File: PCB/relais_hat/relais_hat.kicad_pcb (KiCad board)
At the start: 4 copper layers, 85 x 56 mm, 61 parts, among them J1 Conn_01x03, J10 Conn_01x02, J11 Conn_01x02, J12 Conn_01x03, J13 DB9_Female, J14 Conn_01x02, J15 Conn_01x02, J16 Conn_01x02, J17 Conn_01x02, J18 Conn_01x02, J2 Conn_01x03, J3 Conn_02x04_Odd_Even, J4 Screw_Terminal_01x02, J5 Screw_Terminal_01x02, J6 Screw_Terminal_01x02, J7 Screw_Terminal_01x02, J8 Conn_01x02, J9 Conn_01x02, K1 RELAY-HLS8L-DC3V-S-C(5P-19X15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, K2 RELAY-HLS8L-DC3V-S-C(5P-19X15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, K3 RELAY-HLS8L-DC3V-S-C(5P-19X15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, K4 RELAY-HLS8L-DC3V-S-C(5P-19X15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, P1 Conn_02x20_Odd_Even, Q1 S8050, Q2 S8050, Q3 S8050, Q4 S8050, U1 XC6206P302MR-G, U2 XC6206P302MR-G, U3 XC6206P302MR-G, U4 XC6206P302MR-G

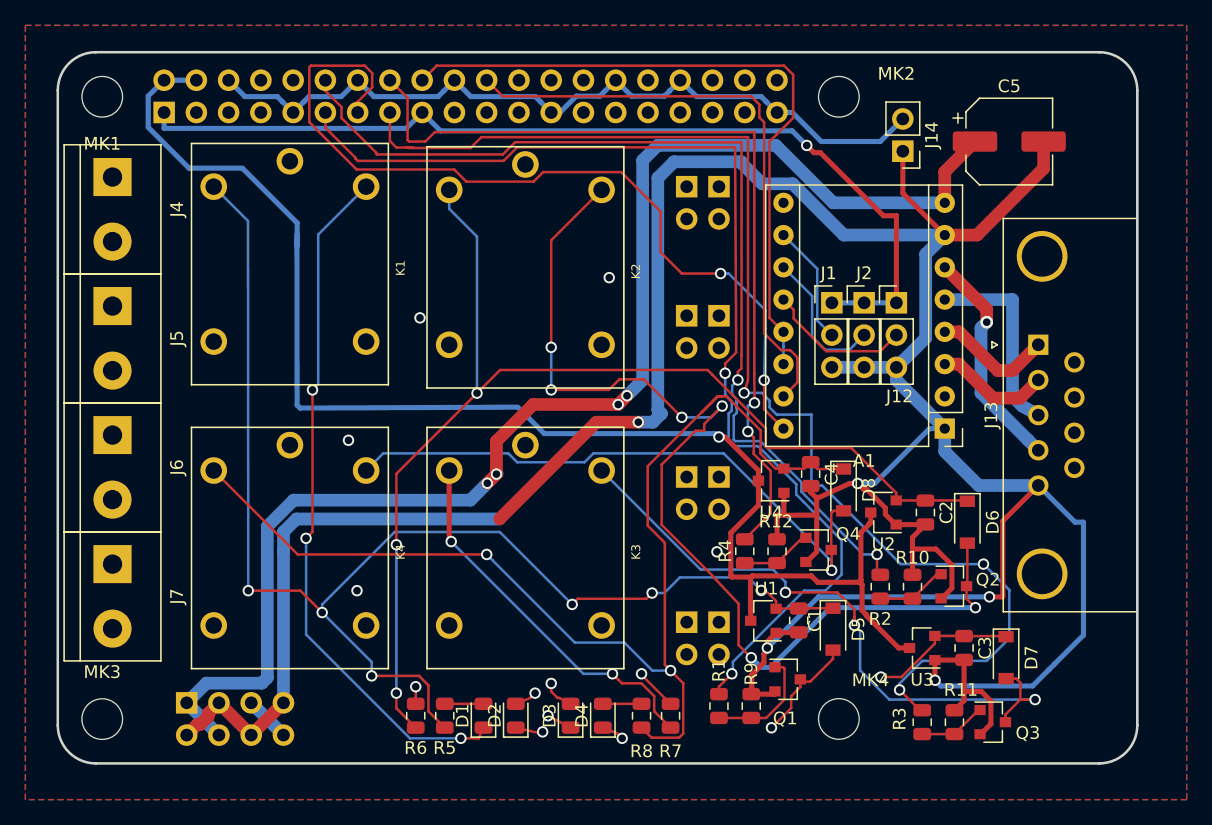
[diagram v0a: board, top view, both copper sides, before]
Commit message: add 3D xt30 model
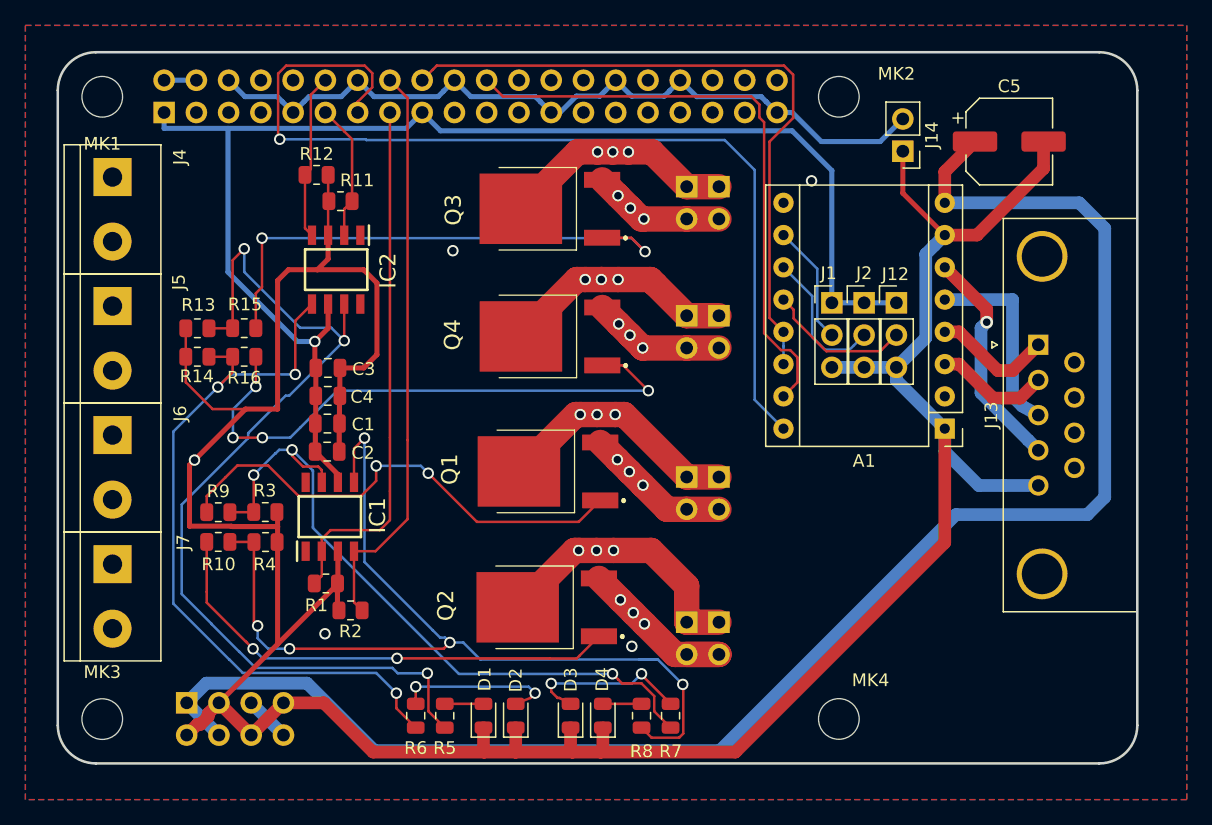
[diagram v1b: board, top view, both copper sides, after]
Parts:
- removed D5, D6, D7, D8: 1N4148W-7-F, Diode_SMD:D_SOD-123
- removed K1, K2, K3, K4: RELAY-HLS8L-DC3V-S-C(5P-19X15MM), relais:REY5-19.0X15.0X15.0MM
- removed U1, U2, U3, U4: XC6206P302MR-G, Package_TO_SOT_SMD:SOT-23
- added IC1: UCC27324D, UCC27324D:SOIC127P600X175-8N, F.Cu at (221.4, 130.3)
- added IC2: UCC27324D, UCC27324D:SOIC127P600X175-8N, F.Cu at (221.9, 110.8)
- added R13: 10k, Resistor_SMD:R_0805_2012Metric, F.Cu at (211.0, 115.4)
- added R14: 10k, Resistor_SMD:R_0805_2012Metric, F.Cu at (211.0, 117.7)
- added R15: 100, Resistor_SMD:R_0805_2012Metric, F.Cu at (214.7, 115.4)
- added R16: 100, Resistor_SMD:R_0805_2012Metric, F.Cu at (214.7, 117.7)
- C1, C3: value 1uF -> 0.1uF
- Q1, Q2, Q3, Q4: value S8050 -> FDD8447L-F085; footprint Package_TO_SOT_SMD:SOT-23 -> FDD8447L:FDD8447LF085
- R1, R2, R3, R4: value 4.7k -> 10k
- R10, R9: value 47k -> 100
- R11, R12: value 47k -> 10k
- moved R11 63.4 mm to (222.3, 105.4), turned to 0 degrees
- moved R10 54.8 mm to (212.7, 132.2), turned to 0 degrees
- moved C3 54.7 mm to (221.3, 118.5), turned to 0 degrees
- moved R3 54.3 mm to (216.3, 129.9), turned to 180 degrees
- moved Q3 53.4 mm to (238.8, 106.0), turned to 90 degrees
- moved C2 47.3 mm to (221.2, 125.1), turned to 0 degrees
- moved R12 46.8 mm to (220.4, 103.3), turned to 0 degrees
- moved R9 44.7 mm to (212.7, 129.9), turned to 0 degrees
- moved R2 41.8 mm to (223.1, 137.6), turned to 180 degrees
- moved C1 40.2 mm to (221.2, 122.9), turned to 0 degrees
- moved C4 38.5 mm to (221.3, 120.8), turned to 0 degrees
- moved R4 37.7 mm to (216.4, 132.3), turned to 0 degrees
- moved R1 32.4 mm to (221.1, 135.5), turned to 180 degrees
- moved Q2 32.0 mm to (238.6, 137.4), turned to 90 degrees
- moved Q4 27.0 mm to (238.8, 116.1), turned to 90 degrees
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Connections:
- A1 pad 2: (no net) -> Net-(A1-Pad2)
- A1 pad 9: (no net) -> Net-(A1-Pad9)
- C1 pad 1: Net-(C1-Pad1) -> +3V3
- C2 pad 1: Net-(C2-Pad1) -> +3V3
- C3 pad 1: Net-(C3-Pad1) -> +3V3
- C4 pad 1: Net-(C4-Pad1) -> +3V3
- D1 pad 1: Net-(D1-Pad1) -> GND
- D2 pad 1: Net-(D2-Pad1) -> GND
- D3 pad 1: Net-(D3-Pad1) -> GND
- D4 pad 1: Net-(D4-Pad1) -> GND
- J13 pad 6: (no net) -> Net-(J13-Pad6)
- J13 pad 7: (no net) -> Net-(J13-Pad7)
- J13 pad 8: (no net) -> Net-(J13-Pad8)
- J13 pad 9: (no net) -> Net-(J13-Pad9)
- P1 pad 10: (no net) -> /UART_RX
- P1 pad 19: (no net) -> /UART_TX_NanopiM4
- P1 pad 21: (no net) -> /UART_RX_NanopiM4
- P1 pad 23: (no net) -> Net-(P1-Pad23)
- P1 pad 24: (no net) -> Net-(P1-Pad24)
- P1 pad 26: (no net) -> Net-(P1-Pad26)
- P1 pad 27: (no net) -> Net-(P1-Pad27)
- P1 pad 28: (no net) -> Net-(P1-Pad28)
- P1 pad 29: (no net) -> Net-(P1-Pad29)
- P1 pad 3: (no net) -> /SDA
- P1 pad 31: (no net) -> Net-(P1-Pad31)
- P1 pad 32: (no net) -> Net-(P1-Pad32)
- P1 pad 33: (no net) -> Net-(P1-Pad33)
- P1 pad 35: (no net) -> Net-(P1-Pad35)
- P1 pad 36: (no net) -> Net-(P1-Pad36)
- P1 pad 37: (no net) -> Net-(P1-Pad37)
- P1 pad 38: (no net) -> Net-(P1-Pad38)
- P1 pad 40: (no net) -> Net-(P1-Pad40)
- P1 pad 5: (no net) -> /SCL
- P1 pad 7: (no net) -> /1-wire
- P1 pad 8: (no net) -> /UART_TX
- Q1 pad 2: GND -> Net-(J16-Pad1)
- Q1 pad 3: Net-(D1-Pad1) -> Net-(J16-Pad2)
- Q2 pad 2: GND -> Net-(J10-Pad1)
- Q2 pad 3: Net-(D2-Pad1) -> Net-(J10-Pad2)
- Q3 pad 2: GND -> Net-(J15-Pad1)
- Q3 pad 3: Net-(D3-Pad1) -> Net-(J15-Pad2)
- Q4 pad 2: GND -> Net-(J11-Pad1)
- Q4 pad 3: Net-(D4-Pad1) -> Net-(J11-Pad2)
- R1 pad 1: /GPIO17 -> GND
- R1 pad 2: Net-(Q1-Pad1) -> /GPIO22
- R10 pad 2: GND -> Net-(IC1-Pad5)
- R11 pad 1: Net-(Q3-Pad1) -> GND
- R11 pad 2: GND -> /GPIO17
- R12 pad 1: Net-(Q4-Pad1) -> /GPIO18
- R2 pad 1: /GPIO18 -> /GPIO23
- R2 pad 2: Net-(Q2-Pad1) -> GND
- R3 pad 1: /GPIO22 -> GND
- R3 pad 2: Net-(Q3-Pad1) -> Net-(IC1-Pad7)
- R4 pad 1: /GPIO23 -> Net-(IC1-Pad5)
- R4 pad 2: Net-(Q4-Pad1) -> GND
- R5 pad 1: Net-(C1-Pad1) -> Net-(IC2-Pad7)
- R6 pad 1: Net-(C2-Pad1) -> Net-(IC2-Pad5)
- R7 pad 1: Net-(C3-Pad1) -> Net-(IC1-Pad7)
- R8 pad 1: Net-(C4-Pad1) -> Net-(IC1-Pad5)
- R9 pad 2: GND -> Net-(IC1-Pad7)
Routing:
- net +5V: track 114.6 -> 2.54 mm, vias 1 -> 0
- net Net-(D2-Pad1): track 106.5 -> 0.00 mm, vias 7 -> 0
- net Net-(C1-Pad1): track 102.7 -> 0.00 mm, vias 6 -> 0
- net Net-(C4-Pad1): track 93.1 -> 0.00 mm, vias 2 -> 0
- net Net-(C2-Pad1): track 91.4 -> 0.00 mm, vias 3 -> 0
- net Net-(D1-Pad1): track 89.5 -> 0.00 mm, vias 4 -> 0
- net /GPIO17: track 88.7 -> 10.8 mm, vias 2 -> 0
- net Net-(D3-Pad1): track 77.3 -> 0.00 mm, vias 4 -> 0
- net Net-(IC1-Pad5): track 0.00 -> 77.0 mm, vias 0 -> 5
- net Net-(IC2-Pad7): track 0.00 -> 75.5 mm, vias 0 -> 3
- net Net-(D4-Pad1): track 74.9 -> 0.00 mm, vias 2 -> 0
- net /GPIO18: track 78.5 -> 13.5 mm, vias 2 -> 0
- net Net-(C3-Pad1): track 64.5 -> 0.00 mm, vias 3 -> 0
- net Net-(IC2-Pad5): track 0.00 -> 59.7 mm, vias 0 -> 3
- net /GPIO22: track 99.5 -> 41.8 mm, vias 3 -> 0
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
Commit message: add temp 1-wire in db9 connector
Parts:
- added R17: 4.7k, Resistor_SMD:R_0805_2012Metric, F.Cu at (266.2, 129.3)
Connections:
- J13 pad 7: Net-(J13-Pad7) -> +3V3
- J13 pad 8: Net-(J13-Pad8) -> /1-wire
- J13 pad 9: Net-(J13-Pad9) -> GND
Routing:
- net /1-wire: track 0.00 -> 127.3 mm, vias 0 -> 3
- net +3V3: track 107.4 -> 142.7 mm
- net GND: track 245.6 -> 249.0 mm
- net /GPIO24: track 54.0 -> 51.2 mm
- net /rpi_gnd: track 62.1 -> 63.9 mm
- net /GPIO25: track 47.4 -> 46.0 mm

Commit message: add R 10k on source/gate
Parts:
- added R18: 10k, Resistor_SMD:R_0805_2012Metric, F.Cu at (251.9, 144.4)
- added R19: 10k, Resistor_SMD:R_0805_2012Metric, F.Cu at (251.5, 133.7)
- added R20: 10k, Resistor_SMD:R_0805_2012Metric, F.Cu at (250.6, 121.3)
- added R21: 10k, Resistor_SMD:R_0805_2012Metric, F.Cu at (251.2, 110.9)
- renumbered Q3 to Q1, Q4 to Q2, Q1 to Q3, Q2 to Q4
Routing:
- net Net-(Q4-Pad1): track 38.2 -> 49.0 mm
- net Net-(Q3-Pad1): track 38.4 -> 48.3 mm
- net Net-(Q1-Pad1): track 41.7 -> 46.4 mm
- net Net-(J11-Pad2): track 54.9 -> 59.5 mm
- net Net-(J16-Pad2): track 56.6 -> 60.8 mm
- net Net-(J15-Pad2): track 54.6 -> 58.7 mm
- net Net-(J10-Pad2): track 58.1 -> 61.7 mm
- net Net-(Q2-Pad1): track 45.9 -> 49.4 mm

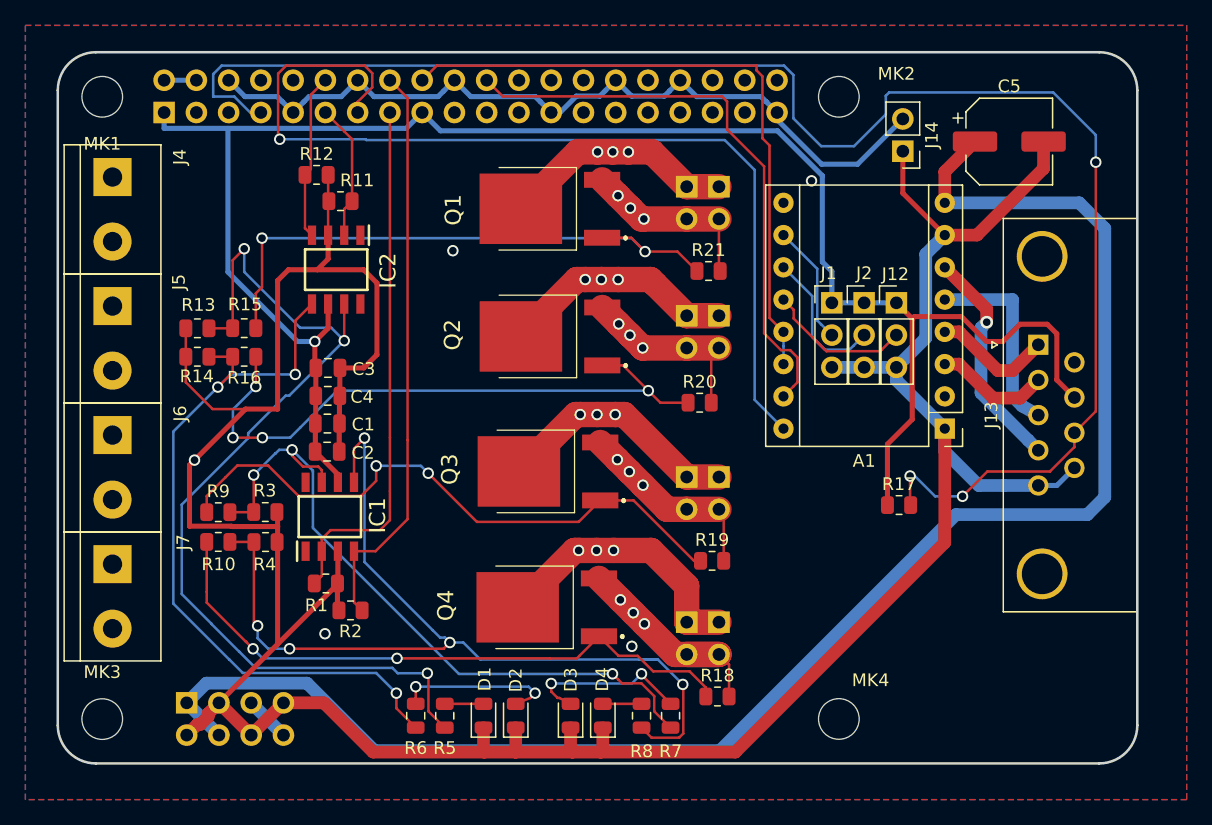
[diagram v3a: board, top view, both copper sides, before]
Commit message: upgrade relais hat and all hat to kicad 7.0
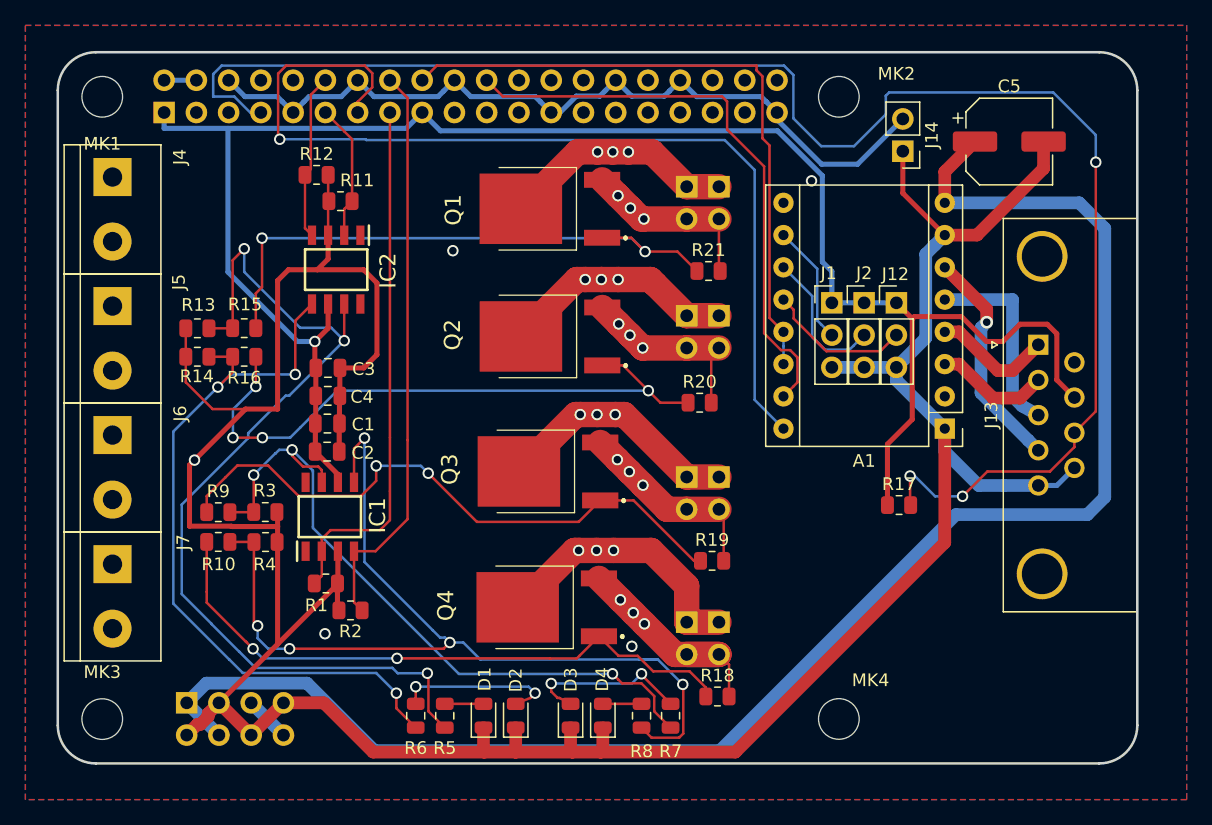
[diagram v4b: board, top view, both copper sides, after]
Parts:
- renumbered C5 to C
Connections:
- net +3V3 renamed +3.3V
- A1 pad 2: Net-(A1-Pad2) -> unconnected-(A1-~{FLT}-Pad2)
- A1 pad 9: Net-(A1-Pad9) -> unconnected-(A1-~{EN}-Pad9)
- IC1 pad 1: Net-(IC1-Pad1) -> unconnected-(IC1-N/A_1-Pad1)
- IC1 pad 8: Net-(IC1-Pad8) -> unconnected-(IC1-N/A_2-Pad8)
- IC2 pad 1: Net-(IC2-Pad1) -> unconnected-(IC2-N/A_1-Pad1)
- IC2 pad 8: Net-(IC2-Pad8) -> unconnected-(IC2-N/A_2-Pad8)
- J13 pad 0: (no net) -> GND
- J13 pad 6: Net-(J13-Pad6) -> unconnected-(J13-Pad6)
- P1 pad 23: Net-(P1-Pad23) -> unconnected-(P1-Pin_23-Pad23)
- P1 pad 24: Net-(P1-Pad24) -> unconnected-(P1-Pin_24-Pad24)
- P1 pad 26: Net-(P1-Pad26) -> unconnected-(P1-Pin_26-Pad26)
- P1 pad 27: Net-(P1-Pad27) -> unconnected-(P1-Pin_27-Pad27)
- P1 pad 28: Net-(P1-Pad28) -> unconnected-(P1-Pin_28-Pad28)
- P1 pad 29: Net-(P1-Pad29) -> unconnected-(P1-Pin_29-Pad29)
- P1 pad 31: Net-(P1-Pad31) -> unconnected-(P1-Pin_31-Pad31)
- P1 pad 32: Net-(P1-Pad32) -> unconnected-(P1-Pin_32-Pad32)
- P1 pad 33: Net-(P1-Pad33) -> unconnected-(P1-Pin_33-Pad33)
- P1 pad 35: Net-(P1-Pad35) -> unconnected-(P1-Pin_35-Pad35)
- P1 pad 36: Net-(P1-Pad36) -> unconnected-(P1-Pin_36-Pad36)
- P1 pad 37: Net-(P1-Pad37) -> unconnected-(P1-Pin_37-Pad37)
- P1 pad 38: Net-(P1-Pad38) -> unconnected-(P1-Pin_38-Pad38)
- P1 pad 40: Net-(P1-Pad40) -> unconnected-(P1-Pin_40-Pad40)
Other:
- net class Default removed
- net class Power removed
